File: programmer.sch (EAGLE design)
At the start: 23 parts, among them IC2 74241, U1 ATMEGA8U2, X2 USB-MICROB, Y1 16MHz

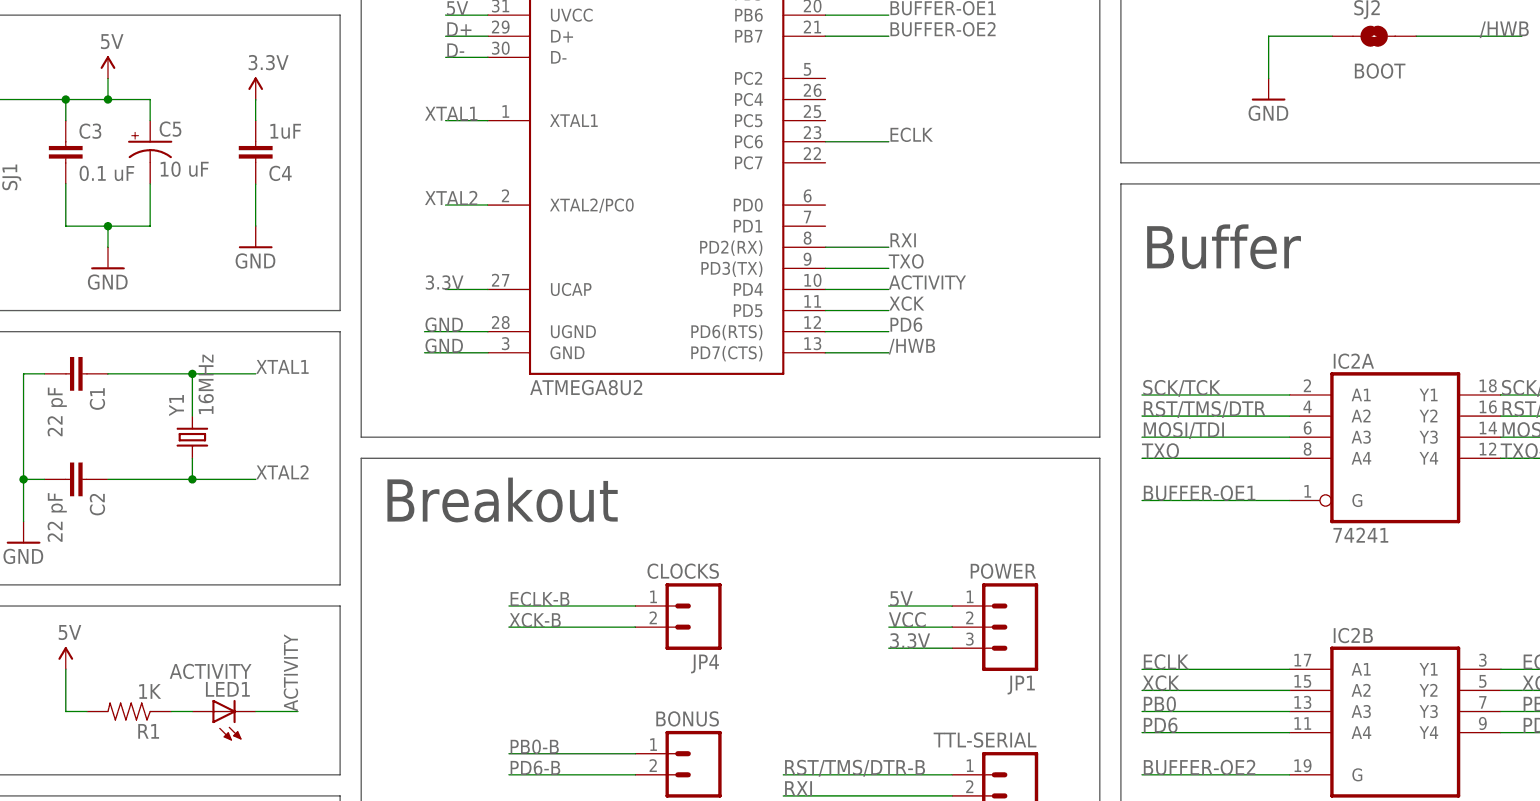
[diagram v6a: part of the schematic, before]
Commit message: Moved all parts to local lbr. IC2->IC1.
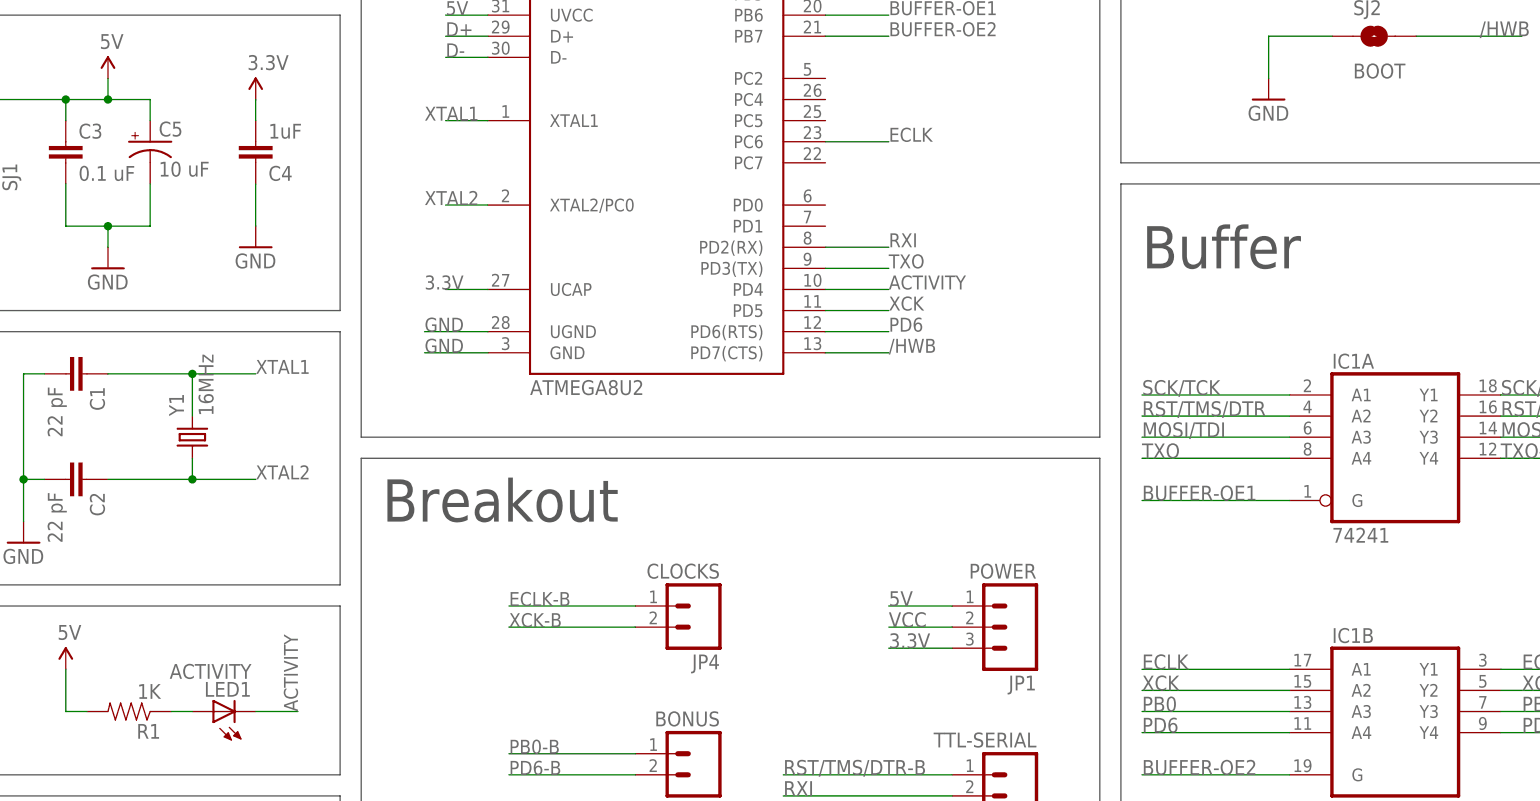
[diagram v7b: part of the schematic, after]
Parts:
- C1, C2, C3, C4: device SparkFun:CAP0805 -> programmer:SPARKFUN_CAP0805
- C5: device SparkFun:CAP_POL1206 -> programmer:SPARKFUN_CAP_POL1206
- ISP, ISP-RA, ISP-SELF: value AVR_SPI_PRG_62X3_LOCK -> SPARKFUN_AVR_SPI_PRG_62X3_LOCK; device SparkFun:AVR_SPI_PRG_62X3_LOCK -> programmer:SPARKFUN_AVR_SPI_PRG_62X3_LOCK
- JP1: device SparkFun:M03LOCK -> programmer:SPARKFUN_M03LOCK
- JP2, JP3: device SparkFun:M06LOCK -> programmer:SPARKFUN_M06LOCK
- R1, R2, R3: device SparkFun:RESISTOR0805-RES -> programmer:SPARKFUN_RESISTOR0805-RES
- SJ1: device SparkFun:SOLDERJUMPERNC -> programmer:SPARKFUN_SOLDERJUMPERNC
- U1: device SparkFun:ATMEGA8U2AU -> programmer:SPARKFUN_ATMEGA8U2AU
- X2: value USB-MICROB -> SPARKFUN_USB-MICROB; device SparkFun:USB-MICROB -> programmer:SPARKFUN_USB-MICROB
- Y1: device SparkFun:CRYSTAL5X3 -> programmer:SPARKFUN_CRYSTAL5X3
- renumbered IC2 to IC1
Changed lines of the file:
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@@
 </classes>
 <parts>
-<part name="U1" library="SparkFun" deviceset="ATMEGA8U2" device="AU" value="ATMEGA8U2"/>
-<part name="C1" library="SparkFun" deviceset="CAP" device="0805" value="22 pF"/>
-<part name="C2" library="SparkFun" deviceset="CAP" device="0805" value="22 pF"/>
-<part name="C3" library="SparkFun" deviceset="CAP" device="0805" value="0.1 uF"/>
+<part name="U1" library="programmer" deviceset="SPARKFUN_ATMEGA8U2" device="AU" value="ATMEGA8U2"/>
+<part name="C1" library="programmer" deviceset="SPARKFUN_CAP" device="0805" value="22 pF"/>
+<part name="C2" library="programmer" deviceset="SPARKFUN_CAP" device="0805" value="22 pF"/>
+<part name="C3" library="programmer" deviceset="SPARKFUN_CAP" device="0805" value="0.1 uF"/>
 <part name="GND2" library="SparkFun" deviceset="GND" device=""/>
 <part name="GND3" library="SparkFun" deviceset="GND" device=""/>
 <part name="GND5" library="SparkFun" deviceset="GND" device=""/>
 <part name="P+1" library="SparkFun" deviceset="VCC" device=""/>
-<part name="R3" library="SparkFun" deviceset="RESISTOR" device="0805-RES" value="22"/>
-<part name="R2" library="SparkFun" deviceset="RESISTOR" device="0805-RES" value="22"/>
-<part name="C4" library="SparkFun" deviceset="CAP" device="0805" value="1uF"/>
+<part name="R3" library="programmer" deviceset="SPARKFUN_RESISTOR" device="0805-RES" value="22"/>
+<part name="R2" library="programmer" deviceset="SPARKFUN_RESISTOR" device="0805-RES" value="22"/>
+<part name="C4" library="programmer" deviceset="SPARKFUN_CAP" device="0805" value="1uF"/>
 <part name="P+5" library="SparkFun" deviceset="3.3V" device=""/>
 <part name="FRAME1" library="frames" deviceset="FRAME_A_L" device="" value="SHEET1"/>
 <part name="GND6" library="SparkFun" deviceset="GND" device=""/>
-<part name="R1" library="SparkFun" deviceset="RESISTOR" device="0805-RES" value="1K"/>
-<part name="C5" library="SparkFun" deviceset="CAP_POL" device="1206" value="10 uF"/>
+<part name="R1" library="programmer" deviceset="SPARKFUN_RESISTOR" device="0805-RES" value="1K"/>
+<part name="C5" library="programmer" deviceset="SPARKFUN_CAP_POL" device="1206" value="10 uF"/>
 <part name="GND1" library="SparkFun" deviceset="GND" device=""/>
 <part name="U$1" library="SparkFun" deviceset="5V" device=""/>
 <part name="U$3" library="SparkFun" deviceset="5V" device=""/>
-<part name="ISP" library="SparkFun" deviceset="AVR_SPI_PRG_6" device="2X3_LOCK" value=""/>
-<part name="ISP-RA" library="SparkFun" deviceset="AVR_SPI_PRG_6" device="2X3_LOCK" value=""/>
-<part name="ISP-SELF" library="SparkFun" deviceset="AVR_SPI_PRG_6" device="2X3_LOCK" value=""/>
-<part name="X2" library="SparkFun" deviceset="USB" device="-MICROB"/>
-<part name="SJ1" library="SparkFun" deviceset="SOLDERJUMPER" device="NC" value="VCC-5V"/>
-<part name="JP2" library="SparkFun" deviceset="M06" device="LOCK" value="JTAG"/>
-<part name="JP3" library="SparkFun" deviceset="M06" device="LOCK" value="TTL-SERIAL"/>
-<part name="Y1" library="SparkFun" deviceset="CRYSTAL" device="5X3" value="16MHz"/>
-<part name="JP1" library="SparkFun" deviceset="M03" device="LOCK" value="POWER"/>
-<part name="IC2" library="programmer" deviceset="74*241" device=""/>
+<part name="ISP" library="programmer" deviceset="SPARKFUN_AVR_SPI_PRG_6" device="2X3_LOCK" value=""/>
+<part name="ISP-RA" library="programmer" deviceset="SPARKFUN_AVR_SPI_PRG_6" device="2X3_LOCK" value=""/>
+<part name="ISP-SELF" library="programmer" deviceset="SPARKFUN_AVR_SPI_PRG_6" device="2X3_LOCK" value=""/>
+<part name="X2" library="programmer" deviceset="SPARKFUN_USB" device="-MICROB"/>
+<part name="SJ1" library="programmer" deviceset="SPARKFUN_SOLDERJUMPER" device="NC" value="VCC-5V"/>
+<part name="JP2" library="programmer" deviceset="SPARKFUN_M06" device="LOCK" value="JTAG"/>
+<part name="JP3" library="programmer" deviceset="SPARKFUN_M06" device="LOCK" value="TTL-SERIAL"/>
+<part name="Y1" library="programmer" deviceset="SPARKFUN_CRYSTAL" device="5X3" value="16MHz"/>
+<part name="JP1" library="programmer" deviceset="SPARKFUN_M03" device="LOCK" value="POWER"/>
+<part name="IC1" library="programmer" deviceset="74*241" device=""/>
 <part name="LED1" library="programmer" deviceset="SPARKFUN_LED" device="" value="ACTIVITY"/>
 <part name="JP4" library="programmer" deviceset="M02" device="LOCK" value="CLOCKS"/>
@@
 <instance part="Y1" gate="G$1" x="-12.7" y="55.88" rot="R90"/>
 <instance part="JP1" gate="G$1" x="86.36" y="33.02" rot="R180"/>
-<instance part="IC2" gate="A" x="132.08" y="55.88"/>
-<instance part="IC2" gate="B" x="132.08" y="22.86"/>
+<instance part="IC1" gate="A" x="132.08" y="55.88"/>
+<instance part="IC1" gate="B" x="132.08" y="22.86"/>
 <instance part="LED1" gate="G$1" x="-10.16" y="22.86" rot="R90"/>
 <instance part="JP4" gate="G$1" x="48.26" y="35.56" rot="R180"/>
@@
 <wire x1="144.78" y1="60.96" x2="160.02" y2="60.96" width="0.1524" layer="91"/>
 <label x="144.78" y="60.96" size="1.778" layer="95" font="vector"/>
-<pinref part="IC2" gate="A" pin="Y1"/>
+<pinref part="IC1" gate="A" pin="Y1"/>
 </segment>
 <segment>
@@
 <wire x1="144.78" y1="58.42" x2="160.02" y2="58.42" width="0.1524" layer="91"/>
 <label x="144.78" y="58.42" size="1.778" layer="95" font="vector"/>
-<pinref part="IC2" gate="A" pin="Y2"/>
+<pinref part="IC1" gate="A" pin="Y2"/>
 </segment>
 <segment>
@@
 <wire x1="144.78" y1="55.88" x2="160.02" y2="55.88" width="0.1524" layer="91"/>
 <label x="144.78" y="55.88" size="1.778" layer="95" font="vector"/>
-<pinref part="IC2" gate="A" pin="Y3"/>
+<pinref part="IC1" gate="A" pin="Y3"/>
 </segment>
 <segment>
@@
 <wire x1="119.38" y1="58.42" x2="101.6" y2="58.42" width="0.1524" layer="91"/>
 <label x="101.6" y="58.42" size="1.778" layer="95" font="vector"/>
-<pinref part="IC2" gate="A" pin="A2"/>
+<pinref part="IC1" gate="A" pin="A2"/>
 </segment>
 </net>
@@
 <wire x1="119.38" y1="60.96" x2="101.6" y2="60.96" width="0.1524" layer="91"/>
 <label x="101.6" y="60.96" size="1.778" layer="95" font="vector"/>
-<pinref part="IC2" gate="A" pin="A1"/>
+<pinref part="IC1" gate="A" pin="A1"/>
 </segment>
 </net>
@@
 <wire x1="119.38" y1="55.88" x2="101.6" y2="55.88" width="0.1524" layer="91"/>
 <label x="101.6" y="55.88" size="1.778" layer="95" font="vector"/>
-<pinref part="IC2" gate="A" pin="A3"/>
+<pinref part="IC1" gate="A" pin="A3"/>
 </segment>
 </net>
@@
 <wire x1="101.6" y1="48.26" x2="119.38" y2="48.26" width="0.1524" layer="91"/>
 <label x="101.6" y="48.26" size="1.778" layer="95" font="vector"/>
-<pinref part="IC2" gate="A" pin="G"/>
+<pinref part="IC1" gate="A" pin="G"/>
 </segment>
 </net>
@@
 <wire x1="119.38" y1="53.34" x2="101.6" y2="53.34" width="0.1524" layer="91"/>
 <label x="101.6" y="53.34" size="1.778" layer="95" font="vector"/>
-<pinref part="IC2" gate="A" pin="A4"/>
+<pinref part="IC1" gate="A" pin="A4"/>
 </segment>
 <segment>
@@
 <wire x1="144.78" y1="53.34" x2="160.02" y2="53.34" width="0.1524" layer="91"/>
 <label x="144.78" y="53.34" size="1.778" layer="95" font="vector"/>
-<pinref part="IC2" gate="A" pin="Y4"/>
+<pinref part="IC1" gate="A" pin="Y4"/>
 </segment>
 <segment>
@@
 </segment>
 <segment>
-<pinref part="IC2" gate="B" pin="A1"/>
+<pinref part="IC1" gate="B" pin="A1"/>
 <wire x1="119.38" y1="27.94" x2="101.6" y2="27.94" width="0.1524" layer="91"/>
 <label x="101.6" y="27.94" size="1.778" layer="95" font="vector"/>
@@
 </segment>
 <segment>
-<pinref part="IC2" gate="B" pin="A3"/>
+<pinref part="IC1" gate="B" pin="A3"/>
 <wire x1="119.38" y1="22.86" x2="101.6" y2="22.86" width="0.1524" layer="91"/>
 <label x="101.6" y="22.86" size="1.778" layer="95" font="vector"/>
@@
 <wire x1="119.38" y1="15.24" x2="101.6" y2="15.24" width="0.1524" layer="91"/>
 <label x="101.6" y="15.24" size="1.778" layer="95" font="vector"/>
-<pinref part="IC2" gate="B" pin="G"/>
+<pinref part="IC1" gate="B" pin="G"/>
 </segment>
 </net>
@@
 </segment>
 <segment>
-<pinref part="IC2" gate="B" pin="A2"/>
+<pinref part="IC1" gate="B" pin="A2"/>
 <wire x1="119.38" y1="25.4" x2="101.6" y2="25.4" width="0.1524" layer="91"/>
 <label x="101.6" y="25.4" size="1.778" layer="95" font="vector"/>
@@
 <net name="ECLK-B" class="0">
 <segment>
-<pinref part="IC2" gate="B" pin="Y1"/>
+<pinref part="IC1" gate="B" pin="Y1"/>
 <wire x1="144.78" y1="27.94" x2="160.02" y2="27.94" width="0.1524" layer="91"/>
 <label x="147.32" y="27.94" size="1.778" layer="95" font="vector"/>
@@
 <net name="XCK-B" class="0">
 <segment>
-<pinref part="IC2" gate="B" pin="Y2"/>
+<pinref part="IC1" gate="B" pin="Y2"/>
 <wire x1="144.78" y1="25.4" x2="160.02" y2="25.4" width="0.1524" layer="91"/>
 <label x="147.32" y="25.4" size="1.778" layer="95" font="vector"/>
@@
 <net name="PB0-B" class="1">
 <segment>
-<pinref part="IC2" gate="B" pin="Y3"/>
+<pinref part="IC1" gate="B" pin="Y3"/>
 <wire x1="144.78" y1="22.86" x2="160.02" y2="22.86" width="0.1524" layer="91"/>
 <label x="147.32" y="22.86" size="1.778" layer="95" font="vector"/>
@@
 <net name="PD6" class="0">
 <segment>
-<pinref part="IC2" gate="B" pin="A4"/>
+<pinref part="IC1" gate="B" pin="A4"/>
 <wire x1="119.38" y1="20.32" x2="101.6" y2="20.32" width="0.1524" layer="91"/>
 <label x="101.6" y="20.32" size="1.778" layer="95" font="vector"/>
@@
 <net name="PD6-B" class="1">
 <segment>
-<pinref part="IC2" gate="B" pin="Y4"/>
+<pinref part="IC1" gate="B" pin="Y4"/>
 <wire x1="144.78" y1="20.32" x2="160.02" y2="20.32" width="0.1524" layer="91"/>
 <label x="147.32" y="20.32" size="1.778" layer="95" font="vector"/>
